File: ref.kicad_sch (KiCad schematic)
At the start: 37 parts

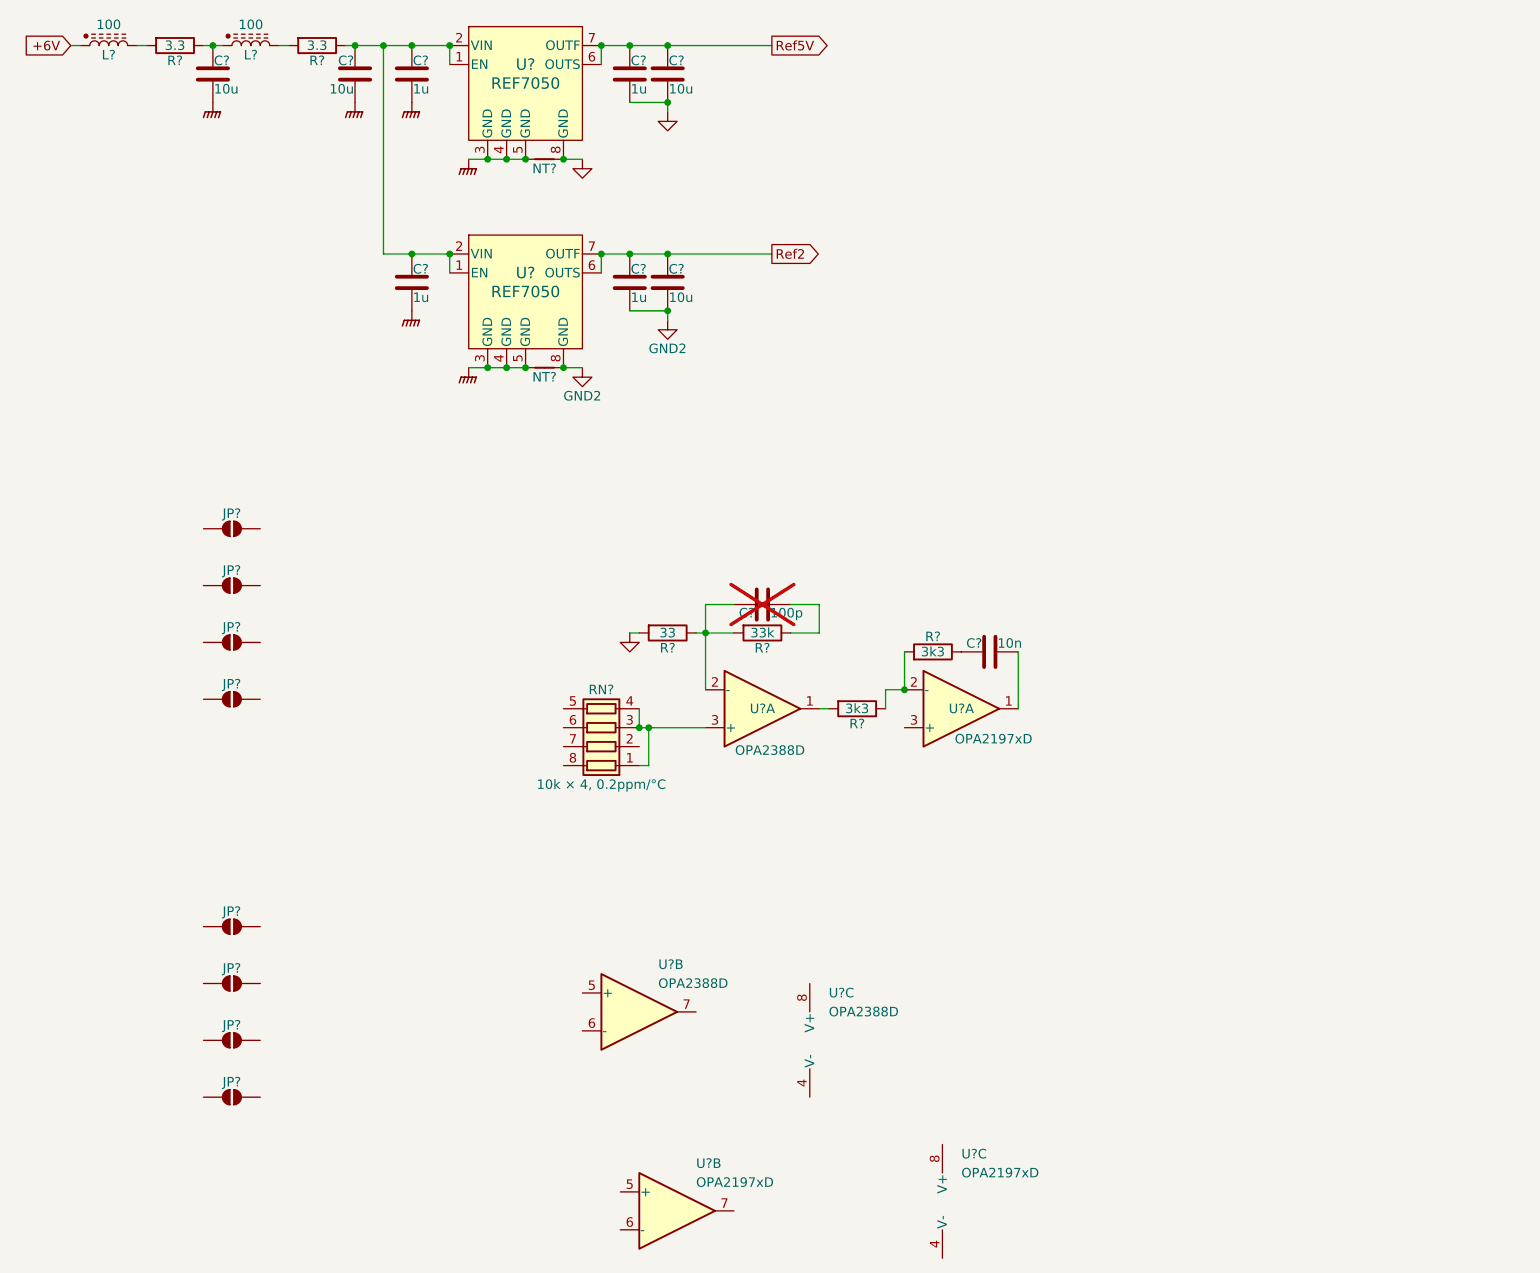
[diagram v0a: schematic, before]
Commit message: Analog side is more or less complete.
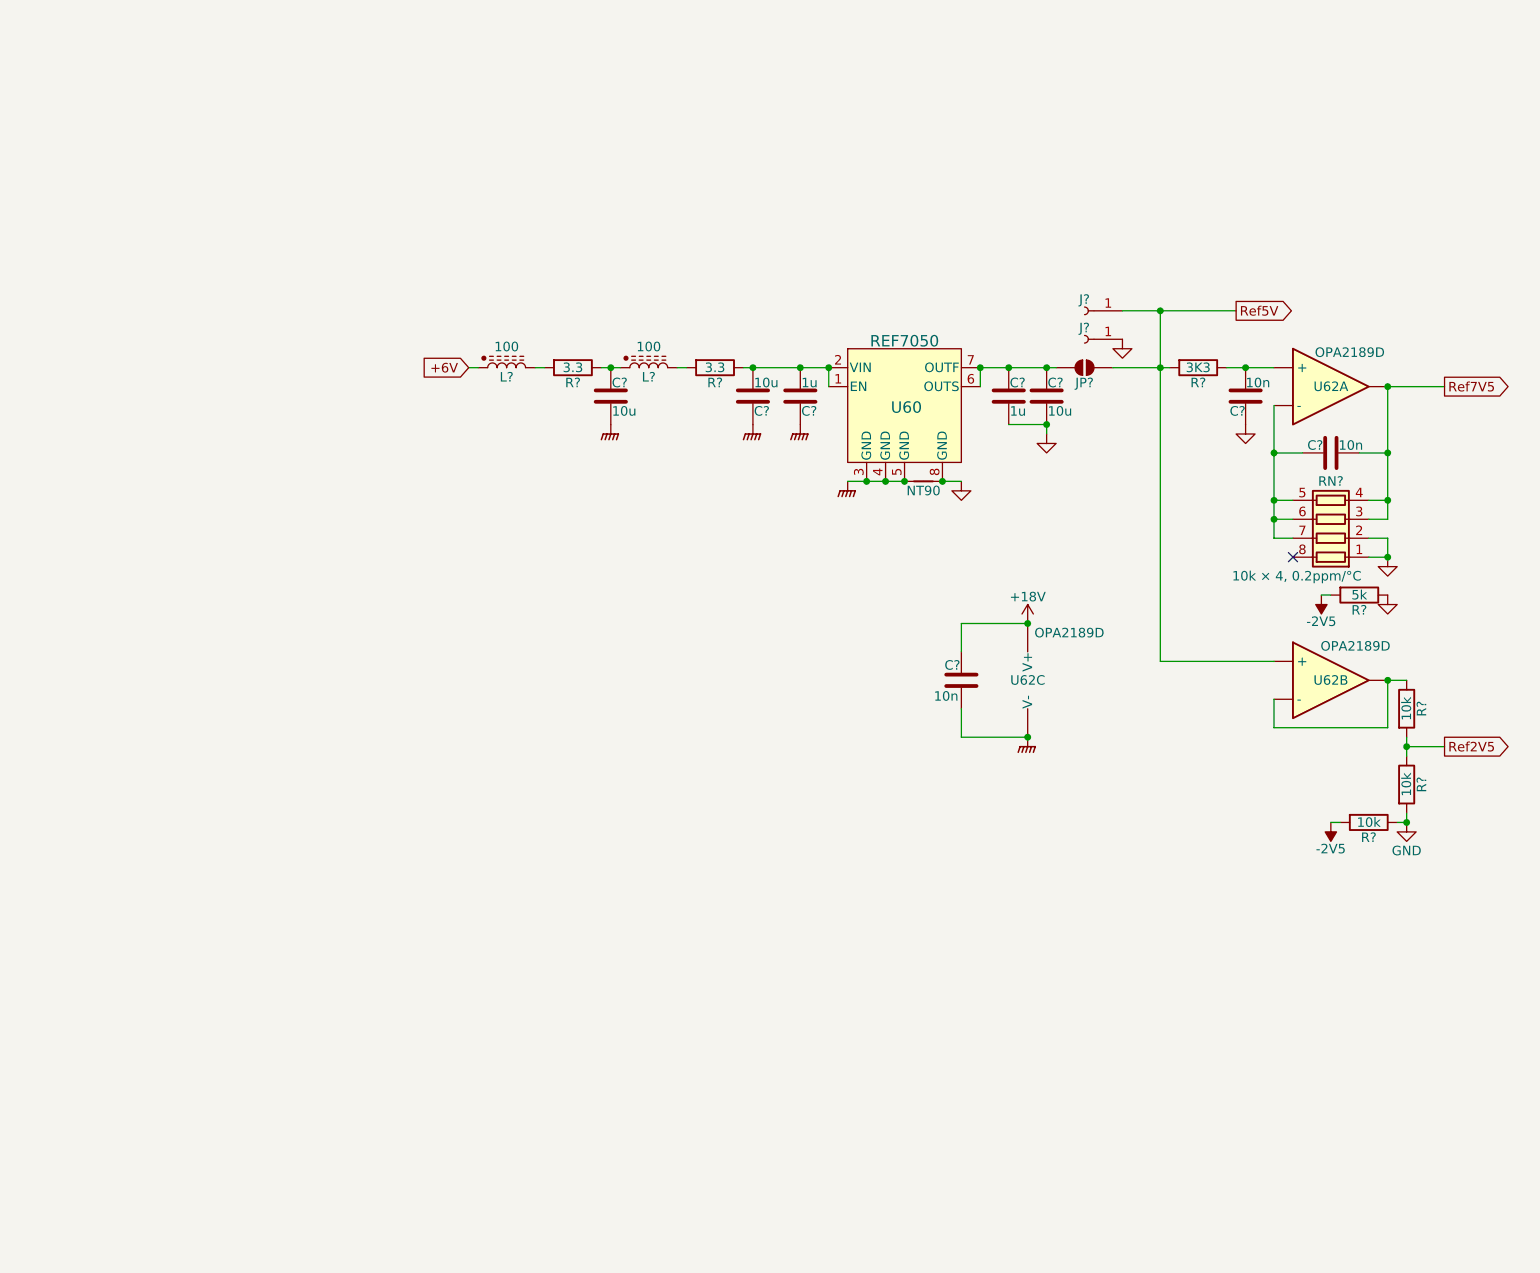
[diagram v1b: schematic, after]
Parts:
- removed C?: 100p, symbol Device:C
- removed C?: 10n, symbol Device:C
- removed C? (x2): 1u, Capacitor_SMD:C_0402_1005Metric, symbol Device:C
- removed C?: 10u, Capacitor_SMD:C_0603_1608Metric, symbol Device:C
- removed JP? (x8): SolderJumper_2_Open, symbol Jumper:SolderJumper_2_Open
- removed NT?: NetTie_2, symbol Device:NetTie_2
- removed R? (x2): 3k3, symbol Device:R
- removed R?: 33, symbol Device:R
- removed R?: 33k, symbol Device:R
- removed RN?: 10k × 4, 0.2ppm/°C, symbol Device:R_Pack04
- removed U? (x3): OPA2197xD, Package_SO:SOIC-8_3.9x4.9mm_P1.27mm, symbol Amplifier_Operational:OPA2197xD
- removed U? (x3): OPA2388D, Package_SO:SOIC-8_3.9x4.9mm_P1.27mm, symbol Parts:OPA2388D
- removed U?: REF7050, FKH0008A-MFG, symbol Parts:REF70
- added C? (x3): 10n, symbol Device:C
- added J? (x2): Conn_01x01_Socket, symbol Connector:Conn_01x01_Socket
- added JP?: SolderJumper_2_Open, symbol Jumper:SolderJumper_2_Open
- added R? (x3): 10k, symbol Device:R
- added R?: 5k, symbol Device:R
- added R?: 3K3, Resistor_SMD:R_0603_1608Metric, symbol Device:R
- added RN?: 10k × 4, 0.2ppm/°C, symbol Device:R_Pack04
- added U62: OPA2189D, Package_SO:SOIC-8_3.9x4.9mm_P1.27mm, symbol Parts:OPA2189D
- gave numbers to parts that had none: 2
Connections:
- net GND: now also C?.2, J?.1 (Pin_1), R?.1, R?.1, R?.2, RN?.1 (R1.1), RN?.2 (R2.1)
- net GNDPWR: now also C?.2, U62.4 (V-)
- net Ref5V: now also J?.1 (Pin_1), JP?.1 (A), R?.2, U62.5 (+); no longer C?.1, C?.1, U60.6 (OUTS), U60.7 (OUTF)
- new net: C?.2, RN?.5 (R4.2), RN?.6 (R3.2), RN?.7 (R2.2), U62.2 (-)
- new net: C?.1, R?.1, U62.3 (+)
- new net: R?.1, U62.6 (-), U62.7
- new net: C?.1, C?.1, JP?.2 (B), U60.6 (OUTS), U60.7 (OUTF)
- new net +18V: C?.1, U62.8 (V+)
- new net -2V5: R?.2, R?.2
- new net Ref2V5: R?.1, R?.2
- new net Ref7V5: C?.1, RN?.3 (R3.1), RN?.4 (R4.1), U62.1
- no-connect marks 0 -> 1
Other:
- moved on the sheet: C?, L?, NT90, R?, U60

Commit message: Little simplifications etc.
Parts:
- removed JP?: SolderJumper_2_Open, symbol Jumper:SolderJumper_2_Open
- added C62: 10u, Capacitor_SMD:C_0603_1608Metric, symbol Device:C
- added L62: 100, symbol Device:L_Ferrite
- added R62: 3.3, Resistor_SMD:R_0603_1608Metric, symbol Device:R
- L61, L63: renamed from L?; symbol Parts:L_Ferrite_Power -> Device:L_Ferrite
- gave numbers to parts that had none: 18
- renumbered NT90 to NT61, U60 to U61
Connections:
- net +6V: no longer L61.1
- net GNDPWR: now also C62.2
- net Ref5V: now also C65.1, C66.1, U61.6 (OUTS), U61.7 (OUTF)
- net at C61.1, R61.1: now also L62.1; no longer L63.1
- new net: C62.1, L63.1, R62.1
- new net: L62.2, R62.2
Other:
- moved on the sheet: C61, C63, C64, C65, C66, C69, J61, J62, L61, L63, NT61, R61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

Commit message: Schematic complete, maybe
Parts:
- removed C63: 10u, Capacitor_SMD:C_0603_1608Metric, symbol Device:C
- removed L63: 100, symbol Device:L_Ferrite
- removed R63: 3.3, Resistor_SMD:R_0603_1608Metric, symbol Device:R
- added TP61: TestPoint, Parts:TestPoint_THTPad_D1.0mm_Drill0.5mm, symbol Connector:TestPoint
- C66: renamed from C67; footprint (none) -> Capacitor_SMD:C_0603_1608Metric; LCSC (none) -> C307500
- C67: renamed from C68; footprint (none) -> Capacitor_SMD:C_0603_1608Metric; LCSC (none) -> C307500
- C68: renamed from C69; footprint (none) -> Capacitor_SMD:C_0603_1608Metric; LCSC (none) -> C307500
- L61, L62: value 100 -> 600; footprint (none) -> Inductor_SMD:L_0603_1608Metric; LCSC (none) -> C1002
- R65: renamed from R66; footprint (none) -> Resistor_SMD:R_0402_1005Metric_Pad0.72x0.64mm_HandSolder; now left out of the parts list
- R66: renamed from R67; footprint (none) -> Resistor_SMD:R_0402_1005Metric_Pad0.72x0.64mm_HandSolder; now left out of the parts list
- RN61: value 10k × 4, 0.2ppm/°C -> 10k × 4; LCSC (none) -> C1358072; now left out of the parts list
- U6: renamed from U61; LCSC (none) -> C6760318
- U61: renamed from U62; LCSC (none) -> C881489; now left out of the parts list
- renumbered C64 to C63, C65 to C64, C66 to C65, R64 to R63, R65 to R64, R68 to R67
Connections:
- net at C63.1, U6.1 (EN), U6.2 (VIN): now also C62.1, R62.1, TP61.1
- net +5V6A: now reaches L61.1
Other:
- moved on the sheet: C61, C62, C66, C67, C68, L61, L62, R61, R62, R63, R64, R65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

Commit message: Part selection
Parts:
- J61, J62: now left out of the parts list
- R61, R62: value 3.3 -> 2R2; LCSC (none) -> C22939; now left out of the parts list
- R63: value 3K3 -> 3k3; LCSC (none) -> C22978
- R64: value 5k -> 4k99; footprint (none) -> Resistor_SMD:R_0603_1608Metric; LCSC (none) -> C22978
- R67: footprint (none) -> Resistor_SMD:R_0402_1005Metric; LCSC (none) -> C25744
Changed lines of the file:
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@@
 			)
 		)
-		(property "Footprint" ""
+		(property "Footprint" "Resistor_SMD:R_0402_1005Metric"
 			(at 196.85 127.762 90)
 			(effects
@@
 			)
 		)
-		(property "Datasheet" ""
+		(property "Datasheet" "~"
 			(at 196.85 129.54 0)
 			(effects
@@
 		(property "Description" "Resistor"
 			(at 196.85 129.54 0)
+			(effects
+				(font
+					(size 1.27 1.27)
+				)
+				(hide yes)
+			)
+		)
+		(property "LCSC" "C25744"
+			(at 196.85 129.54 90)
 			(effects
 				(font
@@
 			)
 		)
-		(property "Value" "5k"
+		(property "Value" "4k99"
 			(at 194.31 99.06 90)
 			(effects
@@
 			)
 		)
-		(property "Footprint" ""
+		(property "Footprint" "Resistor_SMD:R_0603_1608Metric"
 			(at 194.31 97.282 90)
 			(effects
@@
 			)
 		)
+		(property "LCSC" "C22978"
+			(at 194.31 99.06 90)
+			(effects
+				(font
+					(size 1.27 1.27)
+				)
+				(hide yes)
+			)
+		)
 		(pin "2"
 		)
@@
 			)
 		)
-		(property "Value" "3K3"
+		(property "Value" "3k3"
 			(at 173.99 68.58 90)
 			(effects
@@
 		(property "Description" "Resistor"
 			(at 173.99 68.58 0)
+			(effects
+				(font
+					(size 1.27 1.27)
+				)
+				(hide yes)
+			)
+		)
+		(property "LCSC" "C22978"
+			(at 173.99 68.58 90)
 			(effects
 				(font
@@
 		(unit 1)
 		(exclude_from_sim no)
-		(in_bom yes)
+		(in_bom no)
 		(on_board yes)
 		(dnp no)
@@
 			)
 		)
-		(property "Value" "3.3"
+		(property "Value" "2R2"
 			(at 118.11 68.58 90)
 			(effects
@@
 			)
 		)
+		(property "LCSC" "C22939"
+			(at 118.11 68.58 90)
+			(effects
+				(font
+					(size 1.27 1.27)
+				)
+				(hide yes)
+			)
+		)
 		(pin "1"
 		)
@@
 		(unit 1)
 		(exclude_from_sim no)
-		(in_bom yes)
+		(in_bom no)
 		(on_board yes)
 		(dnp no)
@@
 			)
 		)
-		(property "Value" "3.3"
+		(property "Value" "2R2"
 			(at 99.06 68.58 90)
 			(effects
@@
 		(property "Description" "Resistor"
 			(at 99.06 68.58 0)
+			(effects
+				(font
+					(size 1.27 1.27)
+				)
+				(hide yes)
+			)
+		)
+		(property "LCSC" "C22939"
+			(at 99.06 68.58 90)
 			(effects
 				(font
@@
 		(unit 1)
 		(exclude_from_sim no)
-		(in_bom yes)
+		(in_bom no)
 		(on_board yes)
 		(dnp no)
@@
 		(unit 1)
 		(exclude_from_sim no)
-		(in_bom yes)
-		(on_board yes)
-		(dnp no)
+		(in_bom no)
+		(on_board yes)
+		(dnp no)

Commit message: ERC passes.
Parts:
- RN61: value 10k × 4 -> LT5400-1; footprint (none) -> Package_SO:MSOP-8-1EP_3x3mm_P0.65mm_EP1.68x1.88mm; symbol Device:R_Pack04 -> Parts:LT5400; R1 (none) -> 10k; R2 (none) -> 10k; R3 (none) -> 10k; R4 (none) -> 10k; now in the parts list
- TP61: footprint Parts:TestPoint_THTPad_D1.0mm_Drill0.5mm -> Parts:TestPoint; now left out of the parts list
- U6: footprint FKH0008A-MFG -> Parts:FKH0008A-MFG
- U61: value OPA2189D -> OPA2189DGK; footprint Package_SO:SOIC-8_3.9x4.9mm_P1.27mm -> Package_SO:MSOP-8_3x3mm_P0.65mm; symbol Parts:OPA2189D -> Parts:OPA2189DGK
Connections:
- net GND: now also RN61.5, RN61.6; no longer RN61.1 (R1.1), RN61.2 (R2.1)
- net GNDPWR: now also RN61.9
- net Ref7V5: now also RN61.7, RN61.8; no longer RN61.3 (R3.1), RN61.4 (R4.1)
- new net: C67.2, RN61.1, RN61.2, RN61.3, U61.2 (-)
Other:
- moved on the sheet: R64

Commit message: Everything assigned except for wierd shit.
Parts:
- R64: LCSC C22978 -> C23046
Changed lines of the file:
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@@
 			)
 		)
-		(property "LCSC" "C22978"
+		(property "LCSC" "C23046"
 			(at 179.07 97.79 90)
 			(effects

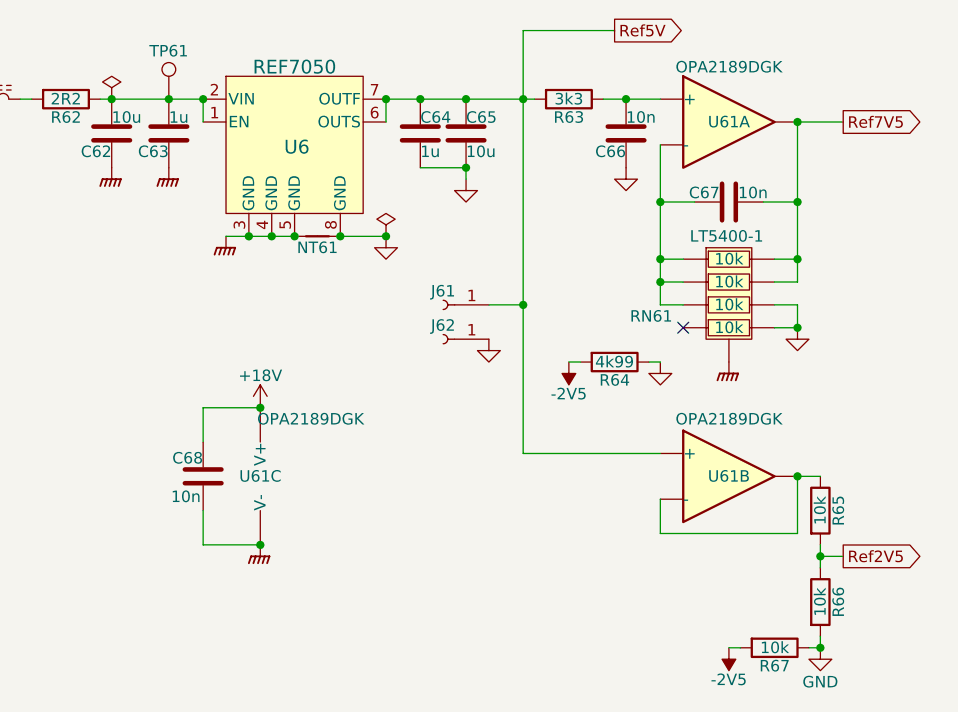
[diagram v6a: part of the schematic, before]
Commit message: Layout underway
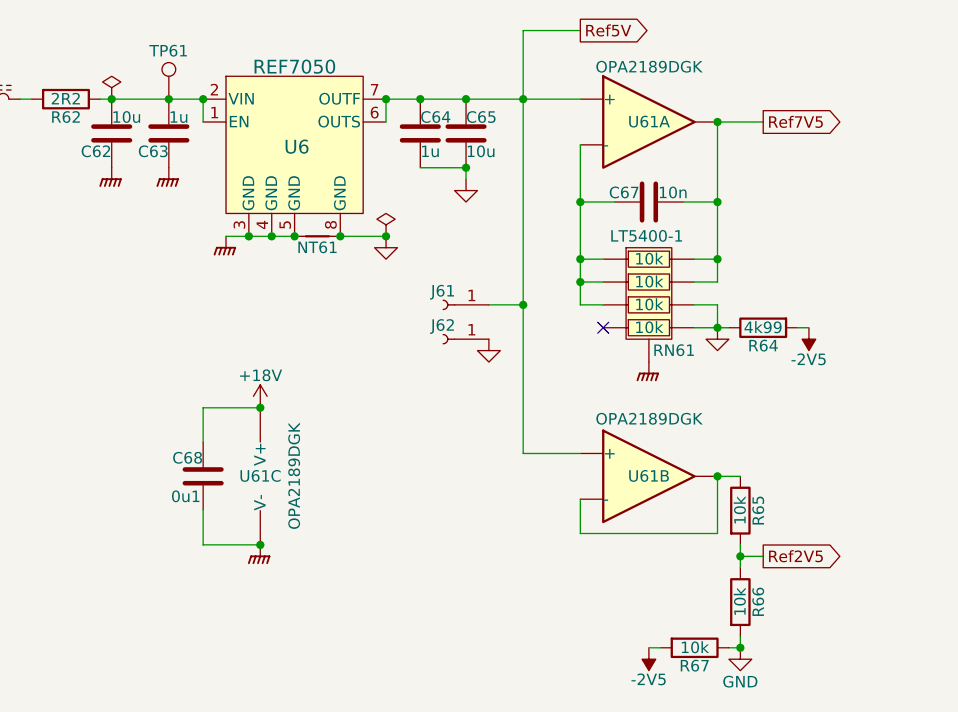
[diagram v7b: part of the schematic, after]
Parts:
- removed C66: 10n, Capacitor_SMD:C_0603_1608Metric, symbol Device:C
- removed R63: 3k3, Resistor_SMD:R_0603_1608Metric, symbol Device:R
- C68: value 10n -> 0u1; footprint Capacitor_SMD:C_0603_1608Metric -> Capacitor_SMD:C_0402_1005Metric; LCSC C307500 -> C307331
- J61, J62: footprint (none) -> TestPoint:TestPoint_Plated_Hole_D5.0mm
- NT61: footprint (none) -> NetTie:NetTie-2_SMD_Pad0.5mm; symbol Device:NetTie_2 -> Parts:NetTie_2
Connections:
- net Ref5V: now also U61.3 (+)
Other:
- moved on the sheet: C67, R64, R65, R66, R67, RN61, U61A, U61B

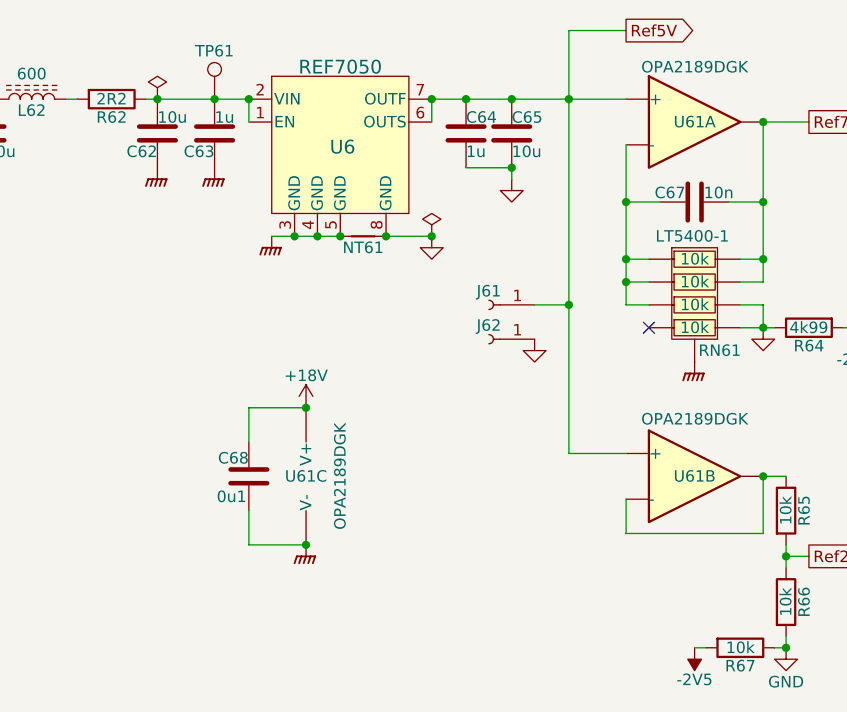
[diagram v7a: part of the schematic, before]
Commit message: Whew.  DACs routed
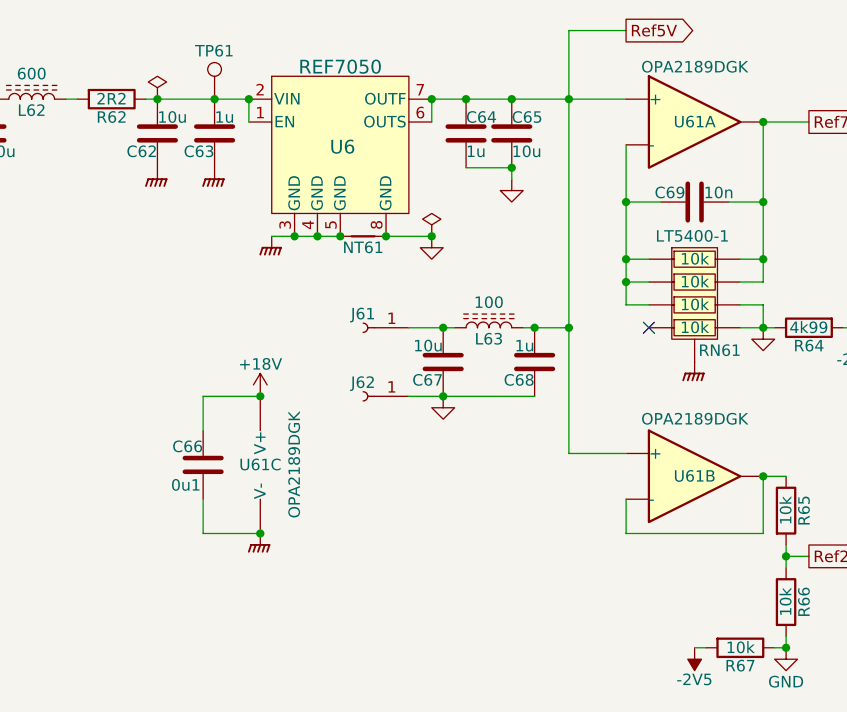
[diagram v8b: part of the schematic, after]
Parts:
- added C67: 10u, Capacitor_SMD:C_0603_1608Metric, symbol Device:C
- added C68: 1u, Capacitor_SMD:C_0402_1005Metric, symbol Device:C
- added L63: 100, Inductor_SMD:L_0603_1608Metric, symbol Device:L_Ferrite
- R67: footprint Resistor_SMD:R_0402_1005Metric -> Resistor_SMD:R_0603_1608Metric; LCSC C25744 -> C25804
- U61: footprint Package_SO:MSOP-8_3x3mm_P0.65mm -> Parts:OPA2189
- renumbered C68 to C66, C67 to C69
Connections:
- net GND: now also C67.2, C68.2
- net Ref5V: now also C68.1, L63.2; no longer J61.1 (Pin_1)
- new net: C67.1, J61.1 (Pin_1), L63.1
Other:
- moved on the sheet: C66, J61, J62, U61C
